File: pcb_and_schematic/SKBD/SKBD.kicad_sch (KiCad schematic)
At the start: 130 parts, among them J1 Conn_01x02, J2 USB_C_Receptacle_USB2.0_14P, SW1 ROT_SKYLOONG_HS, SW10 ROT_SKYLOONG_HS, SW2 ROT_SKYLOONG_HS, SW3 ROT_SKYLOONG_HS, SW4 ROT_SKYLOONG_HS, SW5 ROT_SKYLOONG_HS, SW6 ROT_SKYLOONG_HS, SW7 ROT_SKYLOONG_HS, SW8 ROT_SKYLOONG_HS, SW9 ROT_SKYLOONG_HS, U2 NCP1117-3.3_SOT223, U3 W25Q128JVS, U4 RP2040, Y1 ABM8-272-T3

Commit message: revision
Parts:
- removed J1: Conn_01x02, Connector_PinHeader_2.54mm:PinHeader_1x02_P2.54mm_Vertical, symbol Connector_Generic:Conn_01x02
- added D31, D32, D33, D34, D35: MMBD4148TW, PCM_Package_TO_SOT_SMD_AKL:SOT-363_SC-70-6, symbol PCM_Diode_AKL:MMBD4148TW
- added MX60, MX61, MX62, MX63, MX64, MX65, MX66, MX67, MX68, MX69, MX70, MX71, MX72: MX_SW_HS, PCM_marbastlib-mx:SW_MX_HS_CPG151101S11_1u, symbol PCM_marbastlib-mx:MX_SW_HS_CPG151101S11
- added S2: MX_stab, PCM_marbastlib-mx:STAB_MX_P_2u, symbol PCM_marbastlib-mx:MX_stab
- added SW11: ROT_SKYLOONG_HS, PCM_marbastlib-various:ROT_SKYLOONG_HS-Switch, symbol PCM_marbastlib-various:ROT_SKYLOONG_HS-Switch
- added SW12: Slide_Switch_SPDT_P3mm_10x5x10mm, PCM_SL_Devices:Slide_Switch_SPDT_P3mm_10x5x10mm, symbol PCM_SL_Devices:Slide_Switch_SPDT_P3mm_10x5x10mm
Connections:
- net Col. 1: no longer SW1.C, SW3.C, SW5.C, SW7.C, SW9.C
- net Col. 10: no longer MX21.1, MX33.1, MX45.1, MX56.1, MX9.1
- net Col. 11: no longer MX10.1, MX22.1, MX34.1, MX46.1, MX57.1
- net Col. 12: no longer MX11.1, MX23.1, MX35.1, MX47.1, MX58.1
- net Col. 13: no longer MX12.1, MX24.1, MX36.1, MX48.1, MX59.1
- net Col. 14: no longer SW10.C, SW2.C, SW4.C, SW6.C, SW8.C
- net Col. 2: no longer MX1.1, MX13.1, MX25.1, MX37.1, MX49.1
- net Col. 3: no longer MX14.1, MX2.1, MX26.1, MX38.1, MX50.1
- net Col. 4: no longer MX15.1, MX27.1, MX3.1, MX39.1, MX51.1
- net Col. 5: no longer MX16.1, MX28.1, MX4.1, MX40.1, MX52.1
- net Col. 6: no longer MX17.1, MX29.1, MX41.1, MX5.1, MX53.1
- net Col. 7: no longer MX18.1, MX30.1, MX42.1, MX54.1, MX6.1
- net Col. 8: no longer MX19.1, MX31.1, MX43.1, MX7.1
- net Col. 9: no longer MX20.1, MX32.1, MX44.1, MX55.1, MX8.1
- net GND: now also SW12.2
- net Rot. Enc A1: no longer D1.4 (K3), D6.4 (K3)
- net Rot. Enc A2: no longer D12.4 (K3), D7.4 (K3)
- net Rot. Enc A3: no longer D13.4 (K3), D18.4 (K3)
- net Rot. Enc A4: no longer D19.4 (K3), D24.4 (K3)
- net Rot. Enc A5: no longer D25.4 (K3), D30.4 (K3)
- net Rot. Enc B1: no longer D1.5 (K2), D6.5 (K2)
- net Rot. Enc B2: no longer D12.5 (K2), D7.5 (K2)
- net Rot. Enc B3: no longer D13.5 (K2), D18.5 (K2)
- net Rot. Enc B4: no longer D19.5 (K2), D24.5 (K2)
- net Rot. Enc B5: no longer D25.5 (K2), D30.5 (K2)
- net Row 1: no longer D1.6 (K1), D2.4 (K3), D2.5 (K2), D2.6 (K1), D3.4 (K3), D3.5 (K2), D3.6 (K1), D4.4 (K3), D4.5 (K2), D4.6 (K1), D5.4 (K3), D5.5 (K2), D5.6 (K1), D6.6 (K1)
- net Row 2: no longer D10.4 (K3), D10.5 (K2), D10.6 (K1), D11.4 (K3), D11.5 (K2), D11.6 (K1), D12.6 (K1), D7.6 (K1), D8.4 (K3), D8.5 (K2), D8.6 (K1), D9.4 (K3), D9.5 (K2), D9.6 (K1)
- net Row 3: no longer D13.6 (K1), D14.4 (K3), D14.5 (K2), D14.6 (K1), D15.4 (K3), D15.5 (K2), D15.6 (K1), D16.4 (K3), D16.5 (K2), D16.6 (K1), D17.4 (K3), D17.5 (K2), D17.6 (K1), D18.6 (K1)
- net Row 4: no longer D19.6 (K1), D20.4 (K3), D20.5 (K2), D20.6 (K1), D21.4 (K3), D21.5 (K2), D21.6 (K1), D22.4 (K3), D22.5 (K2), D22.6 (K1), D23.4 (K3), D23.5 (K2), D23.6 (K1), D24.6 (K1)
- net Row 5: no longer D25.6 (K1), D26.4 (K3), D26.5 (K2), D26.6 (K1), D27.4 (K3), D27.5 (K2), D27.6 (K1), D28.4 (K3), D28.5 (K2), D28.6 (K1), D29.4 (K3), D29.5 (K2), D29.6 (K1), D30.6 (K1)
- net ~{USB_BOOT}: now also SW12.1
- net at MX48.2: now also D23.3 (A3); no longer D23.1 (A1)
- net at MX37.2: now also D20.1 (A1); no longer D20.3 (A3)
- net at D9.1 (A1): now also MX16.2; no longer MX18.2
- net at D9.3 (A3): now also MX18.2; no longer MX16.2
- net at MX30.2: now also D15.3 (A3); no longer D15.1 (A1)
- net at MX42.2: now also D21.3 (A3); no longer D21.1 (A1)
- net at MX25.2: now also D14.1 (A1); no longer D14.3 (A3)
- net at MX46.2: now also D23.1 (A1); no longer D23.3 (A3)
- net at MX28.2: now also D15.1 (A1); no longer D15.3 (A3)
- net at MX31.2: now also D16.1 (A1); no longer D16.3 (A3)
- net at D22.1 (A1): now also MX43.2; no longer MX45.2
- net at D22.3 (A3): now also MX45.2; no longer MX43.2
- net at MX36.2: now also D17.3 (A3); no longer D17.1 (A1)
- net at MX9.2: now also D4.3 (A3); no longer D4.1 (A1)
- net at D10.1 (A1): now also MX19.2; no longer MX21.2
- net at D10.3 (A3): now also MX21.2; no longer MX19.2
- net at D28.3 (A3): now also MX60.2
- net at D2.1 (A1): now also MX1.2; no longer MX3.2
- net at D2.3 (A3): now also MX3.2; no longer MX1.2
- net at MX6.2: now also D3.3 (A3); no longer D3.1 (A1)
- net at MX10.2: now also D5.1 (A1); no longer D5.3 (A3)
- net at MX34.2: now also D17.1 (A1); no longer D17.3 (A3)
- net at D25.1 (A1): now also SW9.A; no longer SW9.S
- net at D25.3 (A3): now also SW9.S; no longer SW9.A
- net at MX33.2: now also D16.3 (A3); no longer D16.1 (A1)
- net at MX12.2: now also D5.3 (A3); no longer D5.1 (A1)
- net at MX27.2: now also D14.3 (A3); no longer D14.1 (A1)
- net at MX13.2: now also D8.1 (A1); no longer D8.3 (A3)
- net at MX39.2: now also D20.3 (A3); no longer D20.1 (A1)
- net at MX7.2: now also D4.1 (A1); no longer D4.3 (A3)
- net Col. 15: now reaches U4.41 (GPIO29_ADC3)
- net at MX4.2: now also D3.1 (A1); no longer D3.3 (A3)
- net at MX22.2: now also D11.1 (A1); no longer D11.3 (A3)
- net at MX15.2: now also D8.3 (A3); no longer D8.1 (A1)
- net at SW10.A: now also D30.1 (A1); no longer D30.3 (A3)
- net at SW10.S: now also D30.3 (A3); no longer D30.1 (A1)
- net at MX24.2: now also D11.3 (A3); no longer D11.1 (A1)
- net at MX40.2: now also D21.1 (A1); no longer D21.3 (A3)
- new net: MX11.1, MX23.1, MX35.1, MX47.1, MX58.1
- new net: MX12.1, MX24.1, MX36.1, MX48.1, MX59.1
- new net: MX18.1, MX30.1, MX42.1, MX54.1, MX6.1, MX61.1, MX64.1, MX67.1, MX70.1
- new net: D34.1 (A1), MX70.2
- new net: MX1.1, MX13.1, MX25.1, MX37.1, MX49.1
- new net: D10.4 (K3), D10.5 (K2), D10.6 (K1), D11.4 (K3), D11.5 (K2), D11.6 (K1), D12.6 (K1), D7.4 (K3), D8.4 (K3), D8.5 (K2), D8.6 (K1), D9.4 (K3), D9.5 (K2), D9.6 (K1)
- new net: MX19.1, MX31.1, MX43.1, MX60.1, MX7.1
- new net: MX14.1, MX2.1, MX26.1, MX38.1, MX50.1
- new net: MX10.1, MX22.1, MX34.1, MX46.1, MX57.1
- new net: MX16.1, MX28.1, MX4.1, MX40.1, MX52.1, MX63.1, MX66.1, MX69.1, MX72.1
- new net: D19.4 (K3), D20.4 (K3), D20.5 (K2), D20.6 (K1), D21.4 (K3), D21.5 (K2), D21.6 (K1), D22.4 (K3), D22.5 (K2), D22.6 (K1), D23.4 (K3), D23.5 (K2), D23.6 (K1), D24.6 (K1)
- new net: D12.4 (K3), D7.6 (K1)
- new net: D12.5 (K2), D32.4 (K3), D32.5 (K2), D32.6 (K1), D7.5 (K2)
- new net: D34.2 (A2), MX71.2
- new net: D34.3 (A3), MX72.2
- new net: D19.5 (K2), D24.5 (K2), D34.4 (K3), D34.5 (K2), D34.6 (K1)
- new net: D13.4 (K3), D14.4 (K3), D14.5 (K2), D14.6 (K1), D15.4 (K3), D15.5 (K2), D15.6 (K1), D16.4 (K3), D16.5 (K2), D16.6 (K1), D17.4 (K3), D17.5 (K2), D17.6 (K1), D18.6 (K1)
- new net: SW10.C, SW2.C, SW4.C, SW6.C, SW8.C
- new net: MX17.1, MX29.1, MX41.1, MX5.1, MX53.1, MX62.1, MX65.1, MX68.1, MX71.1
- new net: D33.2 (A2), MX68.2
- new net: MX20.1, MX32.1, MX44.1, MX55.1, MX8.1
- new net: MX15.1, MX27.1, MX3.1, MX39.1, MX51.1
- new net: MX21.1, MX33.1, MX45.1, MX56.1, MX9.1
- new net: D32.1 (A1), MX64.2
- new net: D32.2 (A2), MX65.2
- new net: D32.3 (A3), MX66.2
- new net: D25.4 (K3), D26.4 (K3), D26.5 (K2), D26.6 (K1), D27.4 (K3), D27.5 (K2), D27.6 (K1), D28.4 (K3), D28.5 (K2), D28.6 (K1), D29.4 (K3), D29.5 (K2), D29.6 (K1), D30.4 (K3), D35.4 (K3)
- new net: SW1.C, SW3.C, SW5.C, SW7.C, SW9.C
- new net: D19.6 (K1), D24.4 (K3)
- new net: D1.4 (K3), D2.4 (K3), D2.5 (K2), D2.6 (K1), D3.4 (K3), D3.5 (K2), D3.6 (K1), D4.4 (K3), D4.5 (K2), D4.6 (K1), D5.4 (K3), D5.5 (K2), D5.6 (K1), D6.6 (K1)
- new net: D25.5 (K2), D30.5 (K2), D35.6 (K1)
- new net: D25.6 (K1), D30.6 (K1), D35.5 (K2)
- new net: D13.6 (K1), D18.4 (K3)
- new net: D13.5 (K2), D18.5 (K2), D33.4 (K3), D33.5 (K2), D33.6 (K1)
- new net: D1.6 (K1), D6.4 (K3)
- new net: D1.5 (K2), D31.4 (K3), D31.5 (K2), D31.6 (K1), D6.5 (K2)
- new net: D33.1 (A1), MX67.2
- new net: D33.3 (A3), MX69.2
- new net: D31.1 (A1), MX61.2
- new net: D31.2 (A2), MX62.2
- new net: D31.3 (A3), MX63.2
- new net: D35.1 (A1), SW11.A
- new net: D35.2 (A2), SW11.B
- new net: D35.3 (A3), SW11.S
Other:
- moved on the sheet: C10, C11, C12, C13, C14, C15, C16, C17, C6, C7, C8, C9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

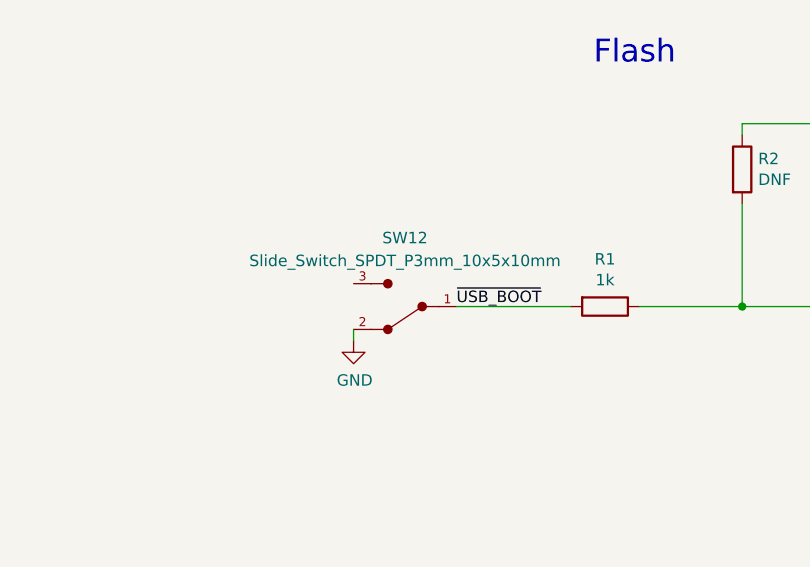
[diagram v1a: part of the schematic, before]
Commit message: wiring update
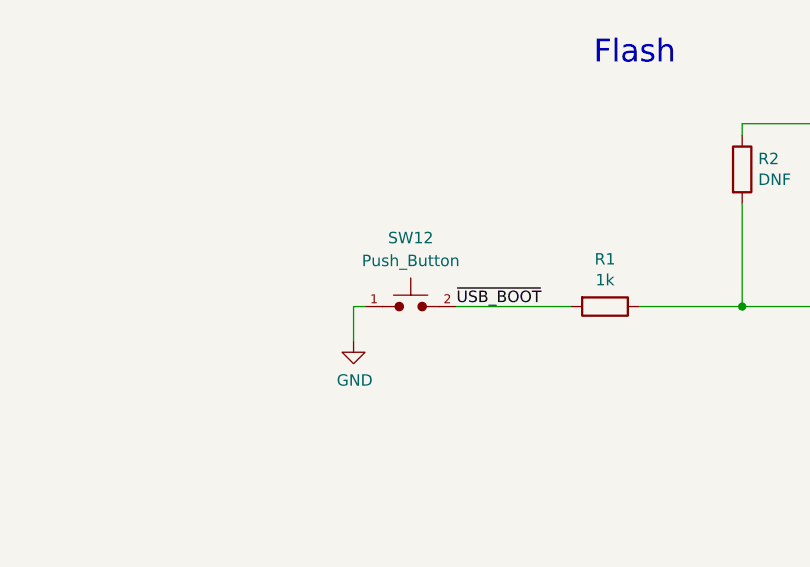
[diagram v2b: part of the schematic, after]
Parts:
- removed SW12: Slide_Switch_SPDT_P3mm_10x5x10mm, PCM_SL_Devices:Slide_Switch_SPDT_P3mm_10x5x10mm, symbol PCM_SL_Devices:Slide_Switch_SPDT_P3mm_10x5x10mm
- added SW12: Push_Button, PCM_marbastlib-various:SW_SPST_SKQG_WithStem, symbol PCM_SL_Devices:Push_Button
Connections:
- net GND: now also SW12.1
- net ~{USB_BOOT}: now also SW12.2
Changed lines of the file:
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@@
 	(wire
 		(pts
+			(xy 222.25 337.82) (xy 220.98 337.82)
+		)
+		(stroke
+			(width 0)
+			(type default)
+		)
+	)
+	(wire
+		(pts
 			(xy 229.87 236.22) (xy 229.87 245.11)
 		)
@@
 	(wire
 		(pts
-			(xy 220.98 340.36) (xy 220.98 341.63)
+			(xy 220.98 337.82) (xy 220.98 341.63)
 		)
 		(stroke
@@
 	)
 	(symbol
+		(lib_id "PCM_SL_Devices:Push_Button")
+		(at 227.33 337.82 0)
+		(unit 1)
+		(exclude_from_sim no)
+		(in_bom yes)
+		(on_board yes)
+		(dnp no)
+		(fields_autoplaced yes)
+		(property "Reference" "SW12"
+			(at 227.33 330.2 0)
+			(effects
+				(font
+					(size 1.27 1.27)
+				)
+			)
+		)
+		(property "Value" "Push_Button"
+			(at 227.33 332.74 0)
+			(effects
+				(font
+					(size 1.27 1.27)
+				)
+			)
+		)
+		(property "Footprint" "PCM_marbastlib-various:SW_SPST_SKQG_WithStem"
+			(at 227.203 340.995 0)
+			(effects
+				(font
+					(size 1.27 1.27)
+				)
+				(hide yes)
+			)
+		)
+		(property "Datasheet" ""
+			(at 227.33 337.82 0)
+			(effects
+				(font
+					(size 1.27 1.27)
+				)
+				(hide yes)
+			)
+		)
+		(property "Description" "Low Profile Switch"
+			(at 227.33 337.82 0)
+			(effects
+				(font
+					(size 1.27 1.27)
+				)
+				(hide yes)
+			)
+		)
+		(pin "1"
+		)
+		(pin "2"
+		)
+		(instances
+			(project ""
+				(path "/913e88b4-4e13-4946-a29a-005665cd01da"
+					(reference "SW12")
+					(unit 1)
+				)
+			)
+		)
+	)
+	(symbol
 		(lib_id "PCM_Diode_AKL:MMBD4148TW")
 		(at 222.25 214.63 90)
@@
 					(unit 1)
 				)
-			)
-		)
-	)
-	(symbol
-		(lib_id "PCM_SL_Devices:Slide_Switch_SPDT_P3mm_10x5x10mm")
-		(at 226.06 337.82 180)
-		(unit 1)
-		(exclude_from_sim no)
-		(in_bom yes)
-		(on_board yes)
-		(dnp no)
-		(fields_autoplaced yes)
-		(property "Reference" "SW12"
-			(at 226.695 330.2 0)
-			(effects
-				(font
-					(size 1.27 1.27)
-				)
-			)
-		)
-		(property "Value" "Slide_Switch_SPDT_P3mm_10x5x10mm"
-			(at 226.695 332.74 0)
-			(effects
-				(font
-					(size 1.27 1.27)
-				)
-			)
-		)
-		(property "Footprint" "PCM_SL_Devices:Slide_Switch_SPDT_P3mm_10x5x10mm"
-			(at 224.79 330.2 0)
-			(effects
-				(font
-					(size 1.27 1.27)
-				)
-				(hide yes)
-			)
-		)
-		(property "Datasheet" ""
-			(at 227.33 344.17 0)
-			(effects
-				(font
-					(size 1.27 1.27)
-				)
-				(hide yes)
-			)
-		)
-		(property "Description" "SPDT Slide Switch with 10mm length, 5mm width and 10mm hight."
-			(at 226.06 337.82 0)
-			(effects
-				(font
-					(size 1.27 1.27)
-				)
-				(hide yes)
-			)
-		)
-		(pin "1"
-		)
-		(pin "3"
-		)
-		(pin "2"
-		)
-		(instances
-			(project ""
-				(path "/913e88b4-4e13-4946-a29a-005665cd01da"
-					(reference "SW12")
-					(unit 1)
-				)

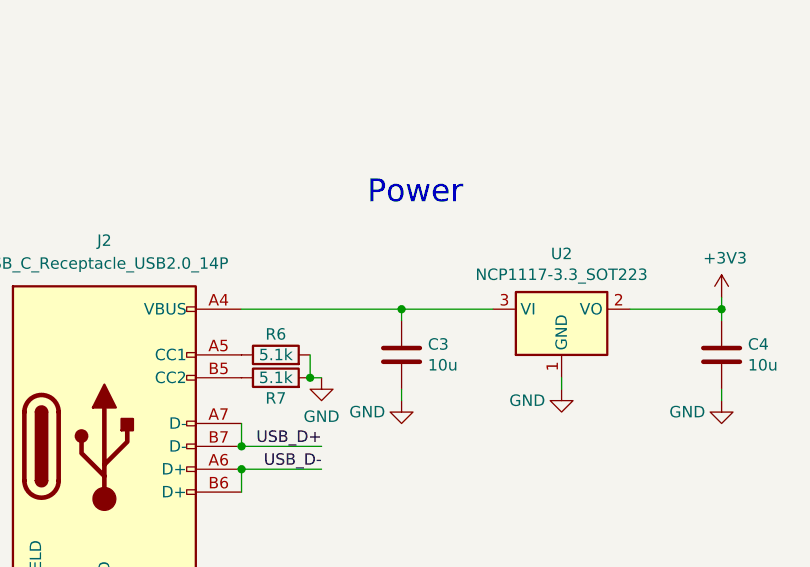
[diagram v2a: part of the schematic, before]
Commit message: wiring change
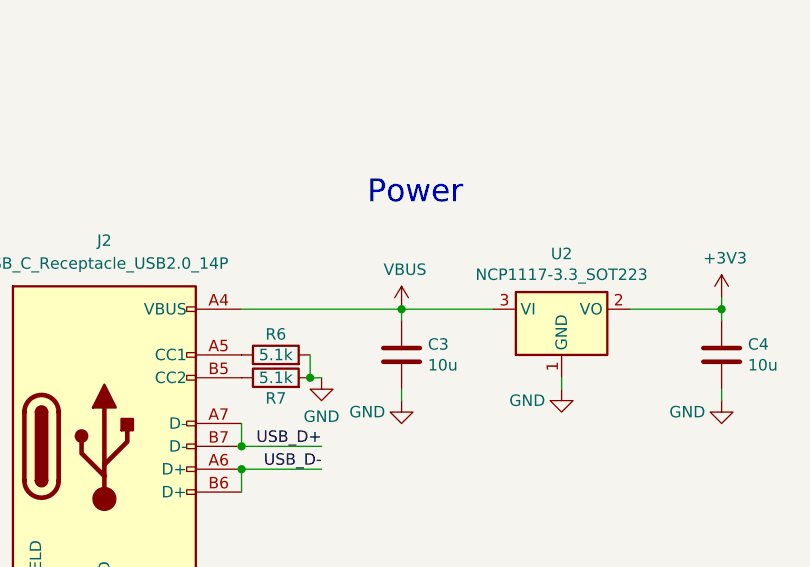
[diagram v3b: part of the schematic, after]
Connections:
- net VBUS: now reaches C3.1, J2.A4 (VBUS), J2.A9 (VBUS), J2.B4 (VBUS), J2.B9 (VBUS), U2.3 (VI)
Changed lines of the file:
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@@
+	)
+	(symbol
+		(lib_id "power:+3V3")
+		(at 114.3 321.31 0)
+		(unit 1)
+		(exclude_from_sim no)
+		(in_bom yes)
+		(on_board yes)
+		(dnp no)
+		(property "Reference" "#PWR04"
+			(at 114.3 325.12 0)
+			(effects
+				(font
+					(size 1.27 1.27)
+				)
+				(hide yes)
+			)
+		)
+		(property "Value" "VBUS"
+			(at 114.681 316.9158 0)
+			(effects
+				(font
+					(size 1.27 1.27)
+				)
+			)
+		)
+		(property "Footprint" ""
+			(at 114.3 321.31 0)
+			(effects
+				(font
+					(size 1.27 1.27)
+				)
+				(hide yes)
+			)
+		)
+		(property "Datasheet" ""
+			(at 114.3 321.31 0)
+			(effects
+				(font
+					(size 1.27 1.27)
+				)
+				(hide yes)
+			)
+		)
+		(property "Description" ""
+			(at 114.3 321.31 0)
+			(effects
+				(font
+					(size 1.27 1.27)
+				)
+				(hide yes)
+			)
+		)
+		(pin "1"
+		)
+		(instances
+			(project "SKBD"
+				(path "/913e88b4-4e13-4946-a29a-005665cd01da"
+					(reference "#PWR04")
+					(unit 1)
+				)
+			)
+		)
 	)
 	(symbol

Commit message: wiring change
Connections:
- net Col. 1: no longer U4.2 (GPIO0)
- net Col. 10: no longer U4.12 (GPIO9)
- net Col. 11: no longer U4.13 (GPIO10)
- net Col. 12: no longer U4.14 (GPIO11)
- net Col. 13: no longer U4.15 (GPIO12)
- net Col. 14: no longer U4.16 (GPIO13)
- net Col. 15: no longer U4.41 (GPIO29_ADC3)
- net Col. 2: no longer U4.3 (GPIO1)
- net Col. 3: no longer U4.4 (GPIO2)
- net Col. 4: no longer U4.5 (GPIO3)
- net Col. 5: no longer U4.6 (GPIO4)
- net Col. 6: no longer U4.7 (GPIO5)
- net Col. 7: no longer U4.8 (GPIO6)
- net Col. 8: no longer U4.9 (GPIO7)
- net Col. 9: no longer U4.11 (GPIO8)
- net Rot. Enc A1: no longer U4.30 (GPIO19)
- net Rot. Enc A2: no longer U4.32 (GPIO21)
- net Rot. Enc A3: no longer U4.35 (GPIO23)
- net Rot. Enc A4: no longer U4.37 (GPIO25)
- net Rot. Enc A5: no longer U4.39 (GPIO27_ADC1)
- net Rot. Enc B1: no longer U4.31 (GPIO20)
- net Rot. Enc B2: no longer U4.34 (GPIO22)
- net Rot. Enc B3: no longer U4.36 (GPIO24)
- net Rot. Enc B4: no longer U4.38 (GPIO26_ADC0)
- net Rot. Enc B5: no longer U4.40 (GPIO28_ADC2)
- net Row 1: now also D1.4 (K3), D2.4 (K3), D2.5 (K2), D2.6 (K1), D3.4 (K3), D3.5 (K2), D3.6 (K1), D4.4 (K3), D4.5 (K2), D4.6 (K1), D5.4 (K3), D5.5 (K2), D5.6 (K1), D6.6 (K1), U4.2 (GPIO0); no longer U4.17 (GPIO14)
- net Row 2: no longer U4.18 (GPIO15)
- net Row 3: no longer U4.27 (GPIO16)
- net Row 4: no longer U4.28 (GPIO17)
- net Row 5: no longer U4.29 (GPIO18)
